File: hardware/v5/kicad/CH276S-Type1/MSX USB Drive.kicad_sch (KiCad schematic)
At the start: 11 parts, among them J1 AVR-JTAG-10, J2 Conn_02x08_Odd_Even, SW1 SK12D07VG4, U2 EPM7064STC44-7, U3 M29F400M

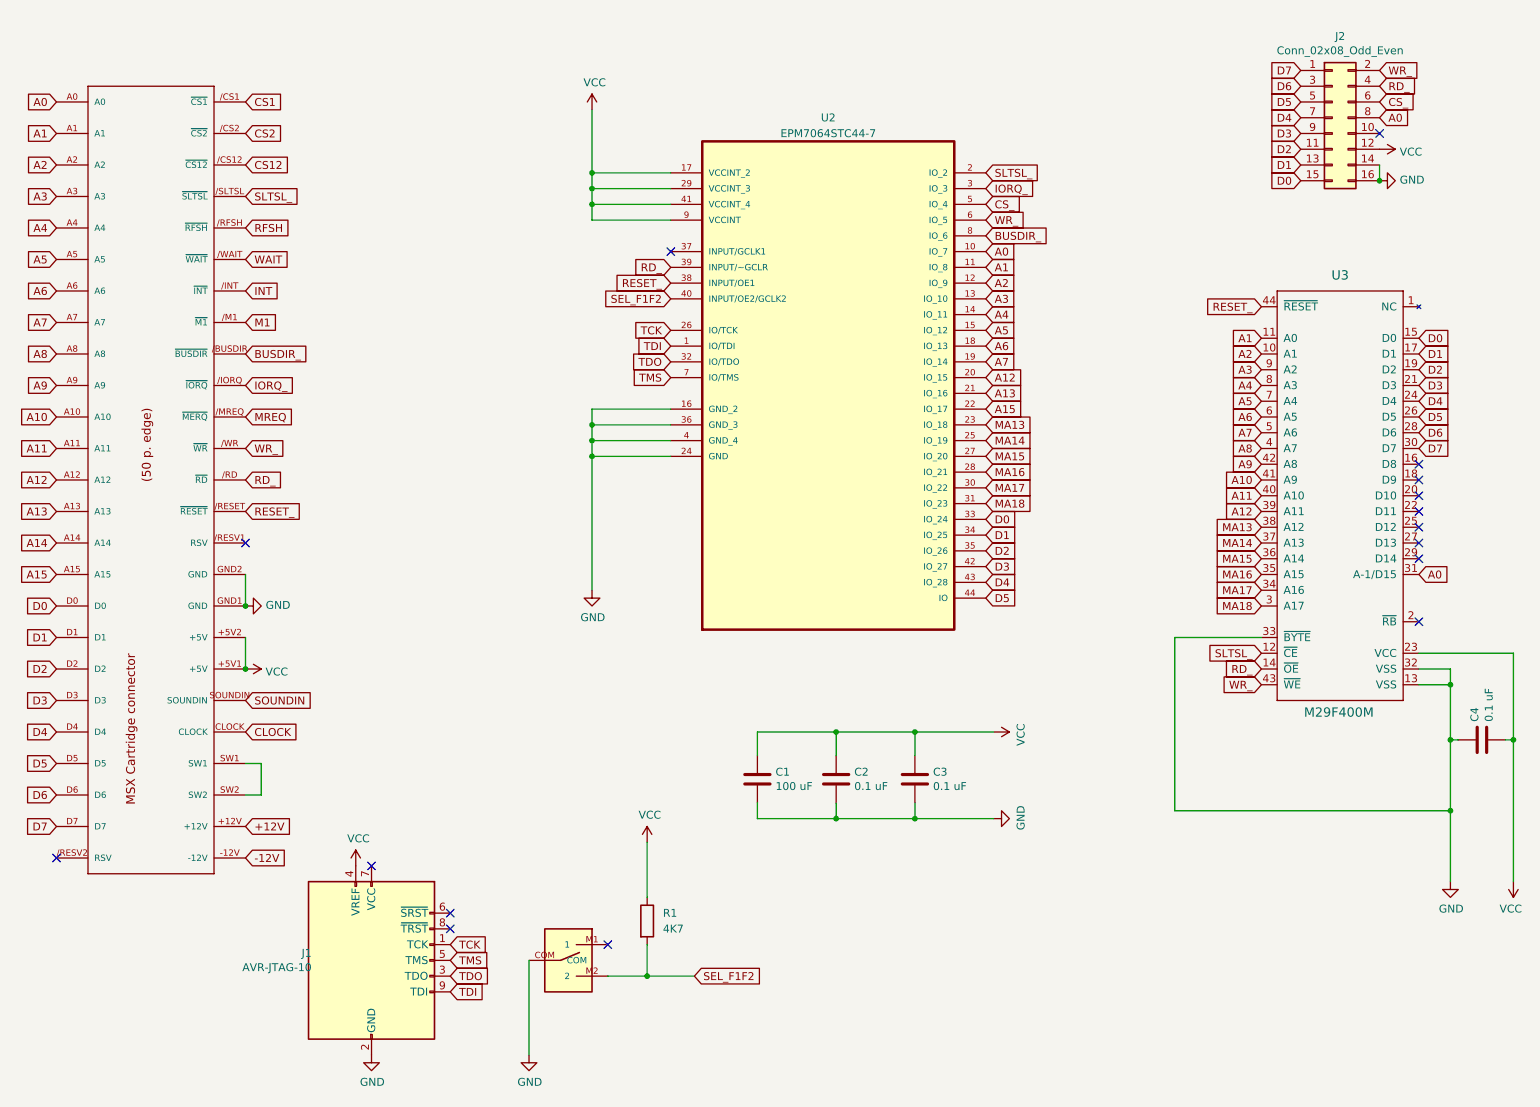
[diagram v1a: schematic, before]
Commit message: PCB adjustments for v5
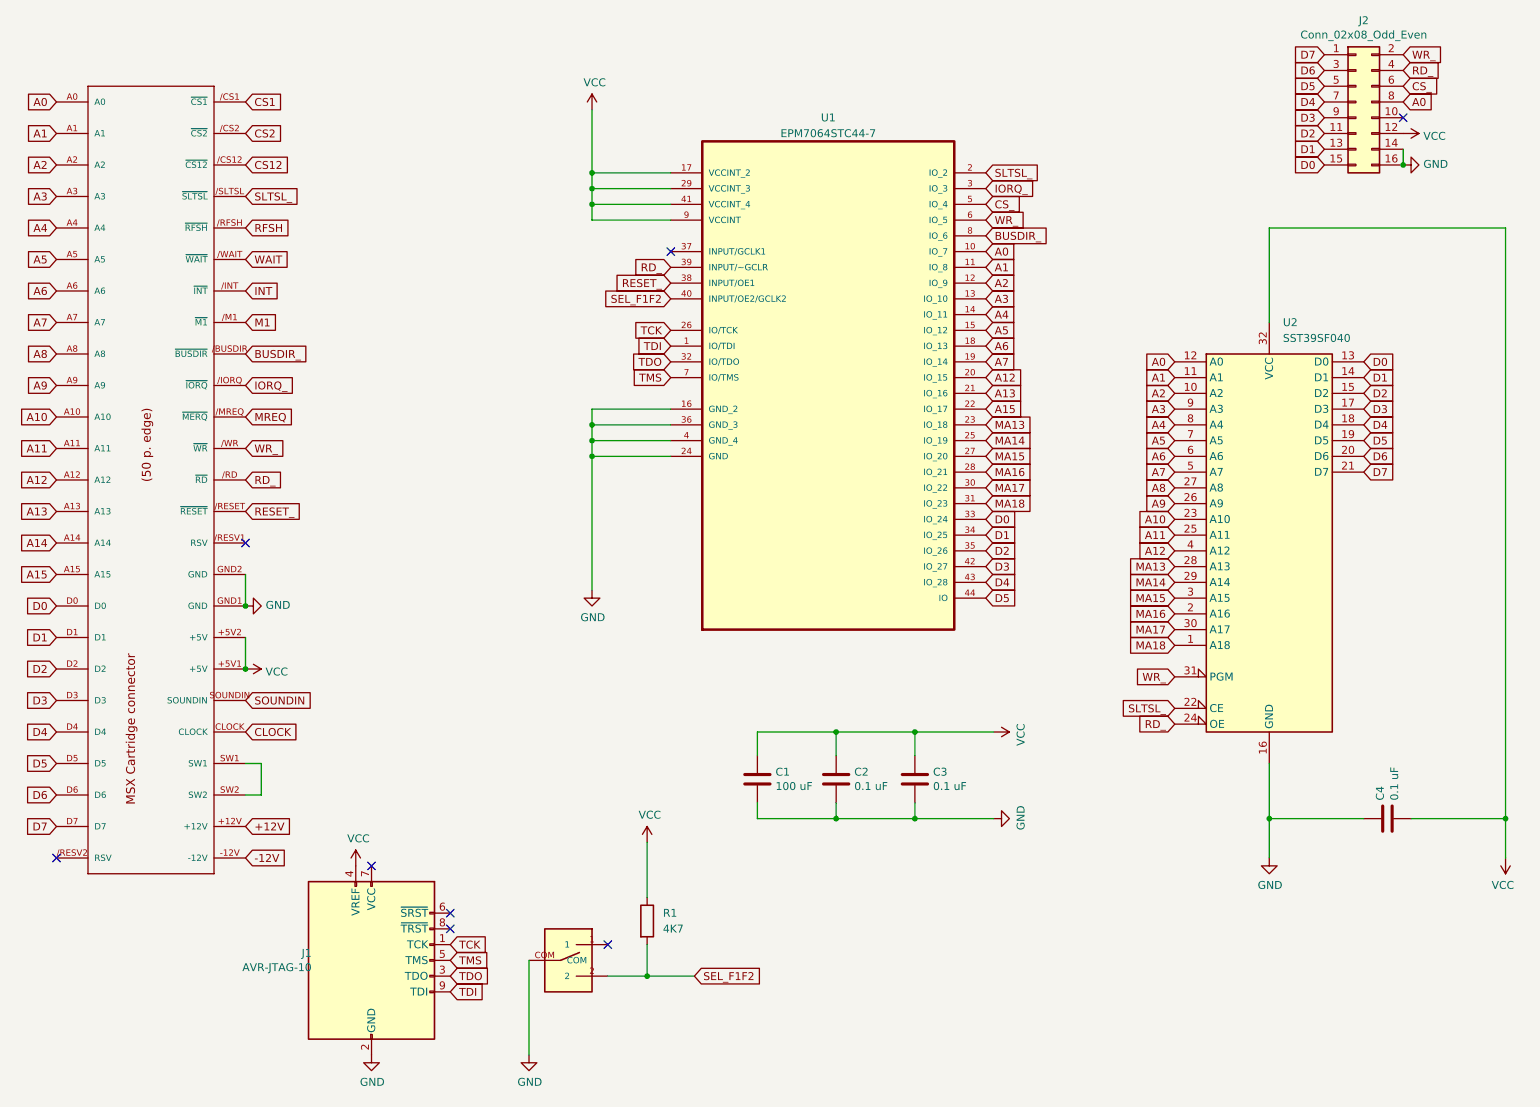
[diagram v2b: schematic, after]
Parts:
- removed U3: M29F400M, libraries:SO44, symbol m29f400m:M29F400M
- added U2: SST39SF040, Package_LCC:PLCC-32_THT-Socket, symbol Memory_Flash:SST39SF040
- J2: footprint libraries:PinHeader_2x08_P2.54mm_Vertical -> Connector_PinHeader_2.54mm:PinHeader_2x08_P2.54mm_Vertical
- renumbered U2 to U1
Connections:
- net A0: now also U2.12 (A0)
- net A1: now also U2.11 (A1)
- net A10: now also U2.23 (A10)
- net A11: now also U2.25 (A11)
- net A12: now also U2.4 (A12)
- net A2: now also U2.10 (A2)
- net A3: now also U2.9 (A3)
- net A4: now also U2.8 (A4)
- net A5: now also U2.7 (A5)
- net A6: now also U2.6 (A6)
- net A7: now also U2.5 (A7)
- net A8: now also U2.27 (A8)
- net A9: now also U2.26 (A9)
- net D0: now also U2.13 (D0)
- net D1: now also U2.14 (D1)
- net D2: now also U2.15 (D2)
- net D3: now also U2.17 (D3)
- net D4: now also U2.18 (D4)
- net D5: now also U2.19 (D5)
- net D6: now also U2.20 (D6)
- net D7: now also U2.21 (D7)
- net GND: now also U2.16 (GND)
- net MA13: now also U2.28 (A13)
- net MA14: now also U2.29 (A14)
- net MA15: now also U2.3 (A15)
- net MA16: now also U2.2 (A16)
- net MA17: now also U2.30 (A17)
- net MA18: now also U2.1 (A18)
- net RD_: now also U2.24 (OE)
- net SEL_F1F2: now also SW1.2; no longer SW1.M2 (2)
- net SLTSL_: now also U2.22 (CE)
- net VCC: now also U2.32 (VCC)
- net WR_: now also U2.31 (PGM)
- no-connect marks 16 -> 8

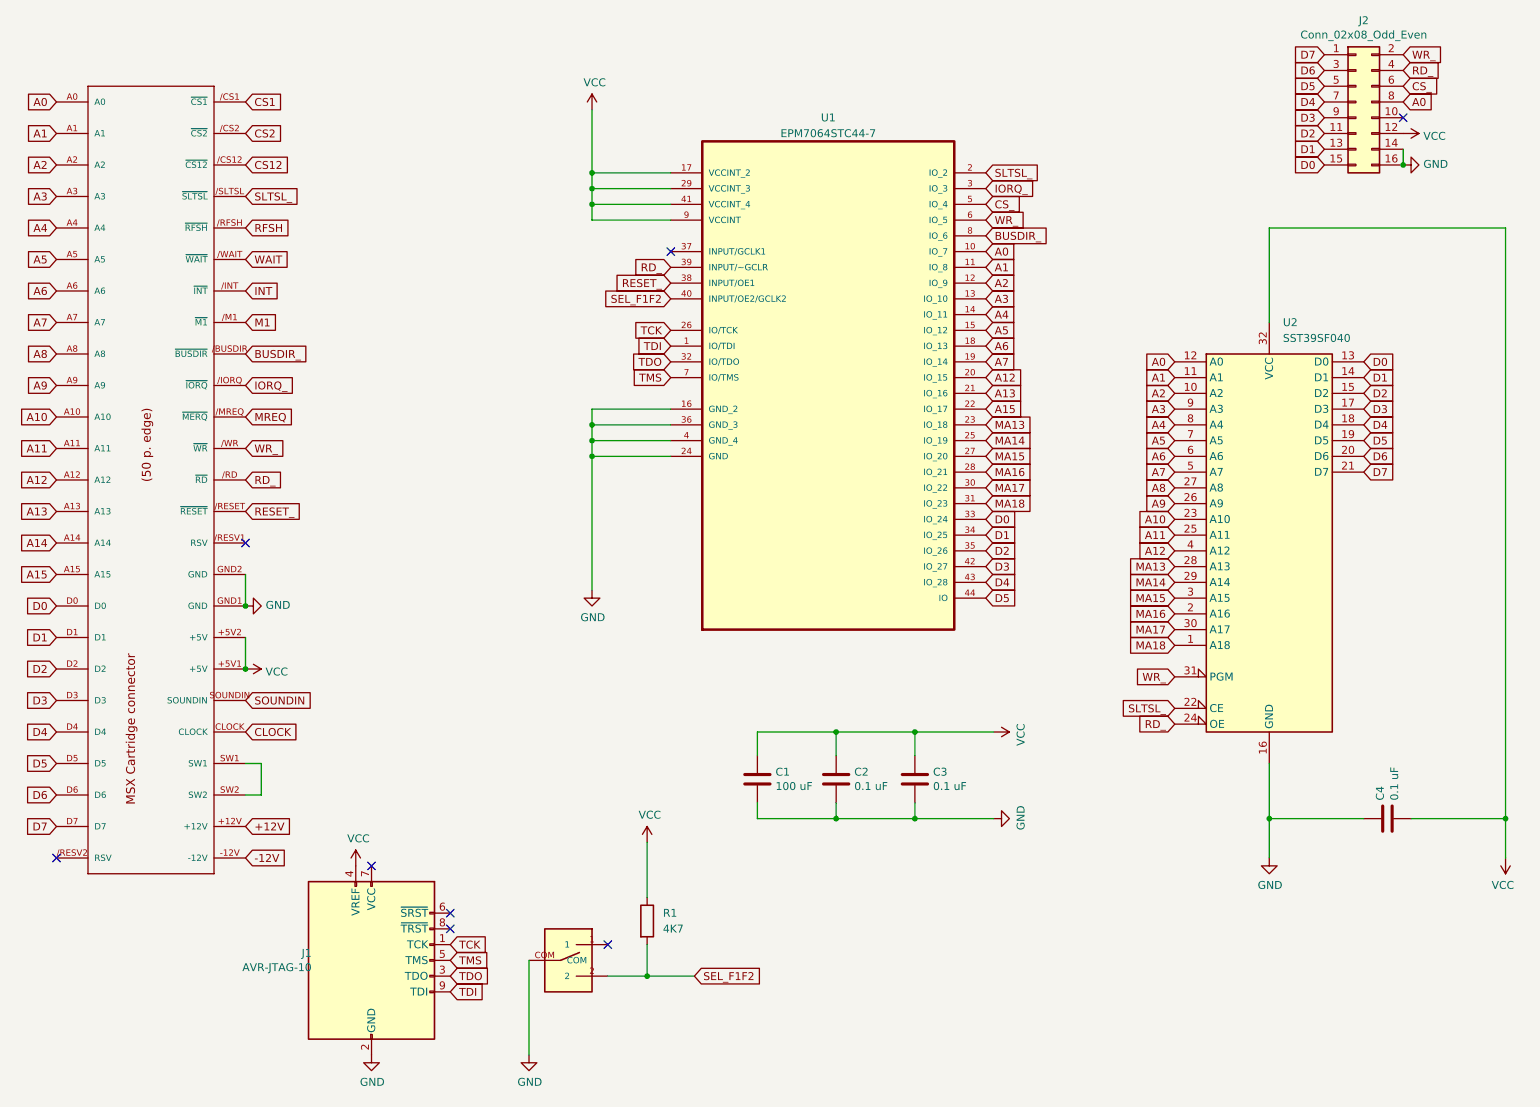
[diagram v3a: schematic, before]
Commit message: fix flash tool, adjustments to v5 pcbs, tests with fusion-c
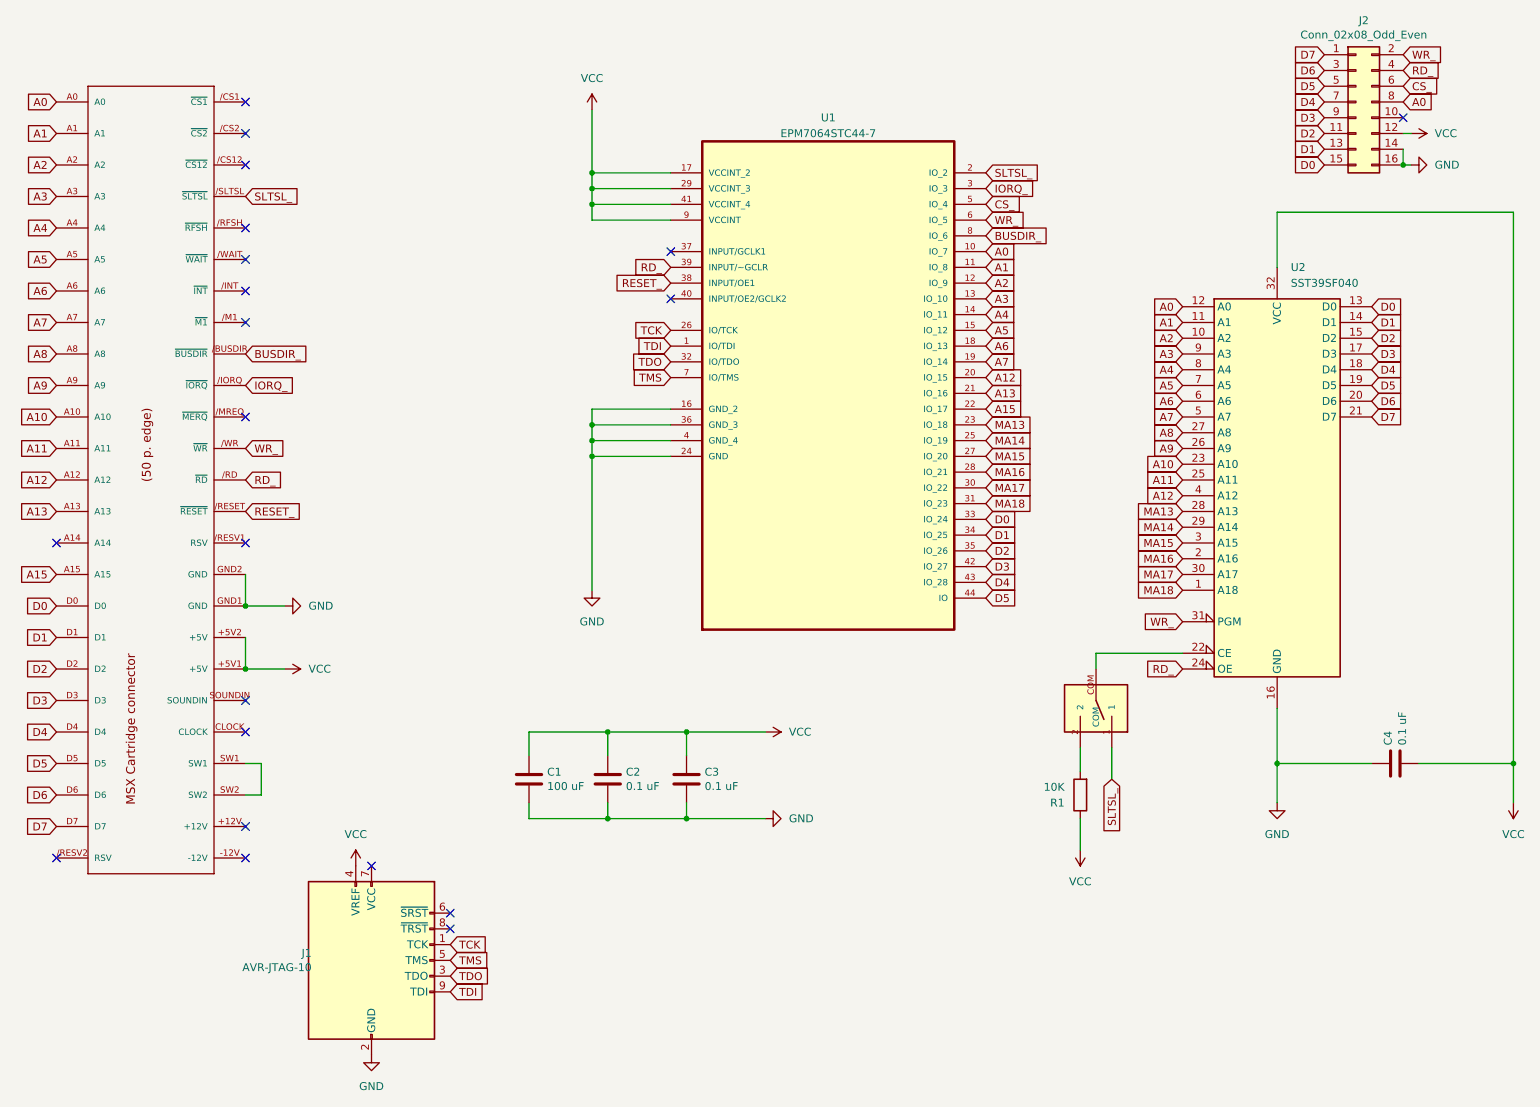
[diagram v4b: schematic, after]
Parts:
- R1: value 4K7 -> 10K
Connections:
- net GND: no longer SW1.COM
- net SLTSL_: now also SW1.1; no longer U2.22 (CE)
- net +12V: no longer names the net of EDG1.+12V
- net -12V: no longer names the net of EDG1.-12V
- net A14: no longer names the net of EDG1.A14
- net CLOCK: no longer names the net of EDG1.CLOCK
- net CS1: no longer names the net of EDG1./CS1 (~{CS1})
- net CS12: no longer names the net of EDG1./CS12 (~{CS12})
- net CS2: no longer names the net of EDG1./CS2 (~{CS2})
- net INT: no longer names the net of EDG1./INT (~{INT})
- net M1: no longer names the net of EDG1./M1 (~{M1})
- net MREQ: no longer names the net of EDG1./MREQ (~{MERQ})
- net RFSH: no longer names the net of EDG1./RFSH (~{RFSH})
- net SEL_F1F2: no longer names the net of R1.2, SW1.2
- net SEL_F1F2: no longer U1.40 (INPUT/OE2/GCLK2)
- net SOUNDIN: no longer names the net of EDG1.SOUNDIN
- net WAIT: no longer names the net of EDG1./WAIT (~{WAIT})
- new net: SW1.COM, U2.22 (CE)
- no-connect marks 8 -> 21
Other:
- moved on the sheet: C1, C2, C3, C4, R1, U2
